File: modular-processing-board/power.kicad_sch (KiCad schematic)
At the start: 10 parts, among them J301 Conn_02x06_Odd_Even, J701 Conn_02x02_Odd_Even, J702 Conn_02x03_Odd_Even, U701 AMS1117-3.3

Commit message: started layout
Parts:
- removed J301: Conn_02x06_Odd_Even, Connector_PinSocket_2.54mm:PinSocket_2x06_P2.54mm_Vertical, symbol Connector_Generic:Conn_02x06_Odd_Even

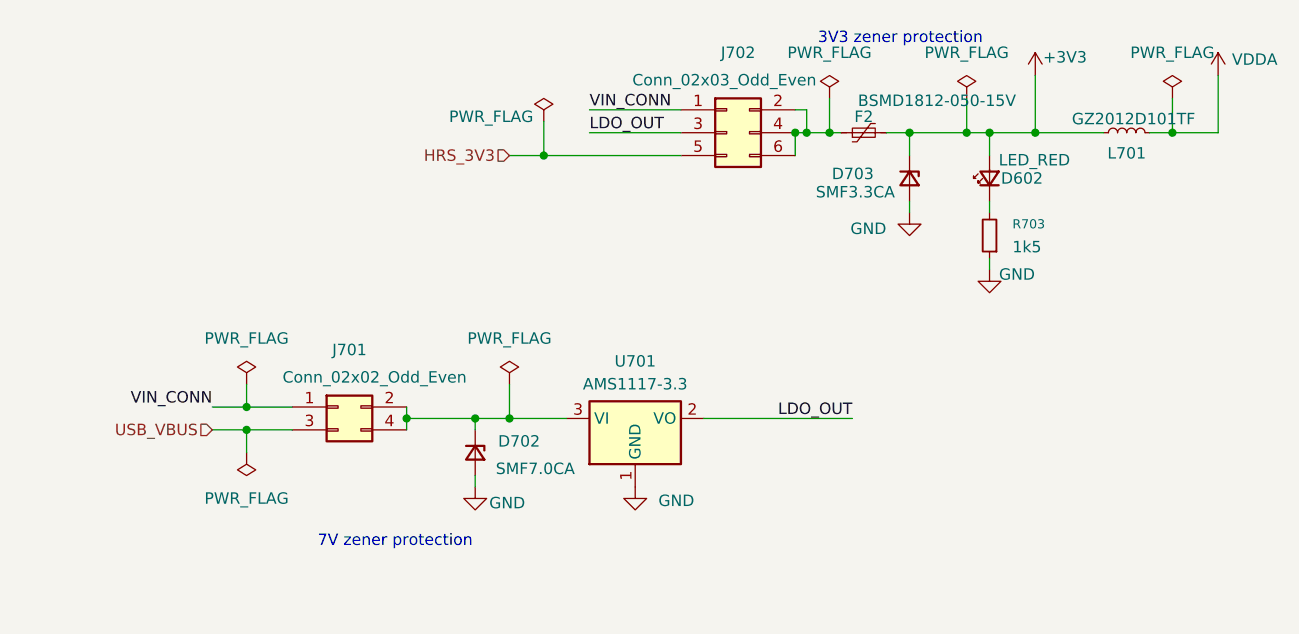
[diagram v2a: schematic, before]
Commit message: removed power input jumpers to single one, added trace impedances and production restrictions (next) route sdram
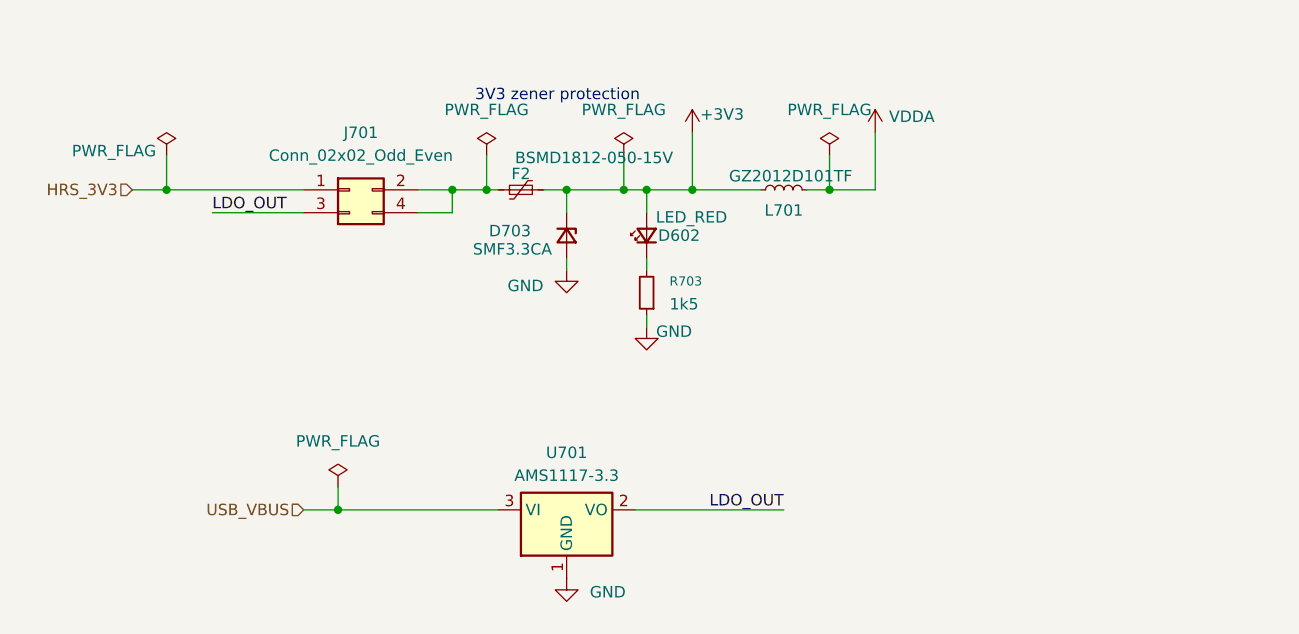
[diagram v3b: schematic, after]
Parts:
- removed D702: SMF7.0CA, Diode_SMD:D_SOD-123F, symbol Device:D_Zener_Small
- removed J702: Conn_02x03_Odd_Even, Connector_PinHeader_2.54mm:PinHeader_2x03_P2.54mm_Vertical, symbol Connector_Generic:Conn_02x03_Odd_Even
- J701: LPN C66690 -> (none); MPN 2.54-2*2PPin -> (none)
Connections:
- net VIN_CONN is gone; now on net HRS_3V3: J701.1 (Pin_1)
- net LDO_OUT: now also J701.3 (Pin_3)
- net USB_VBUS: now also U701.3 (VI); no longer J701.3 (Pin_3)
- net at J701.2 (Pin_2), J701.4 (Pin_4): now also F2.1; no longer U701.3 (VI)
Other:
- note removed: "7V zener protection"
- moved on the sheet: D602, D703, F2, L701, R703, U701

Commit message: figuring out delay matching for sdram
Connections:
- net HRS_3V3: now also J701.3 (Pin_3); no longer J701.1 (Pin_1)
- net LDO_OUT: now also J701.1 (Pin_1); no longer J701.3 (Pin_3)
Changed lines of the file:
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@@
 	)
 	(junction
-		(at 46.99 40.64)
+		(at 46.99 43.18)
 		(diameter 0)
 		(color 0 0 0 0)
@@
 	(wire
 		(pts
-			(xy 43.18 40.64) (xy 46.99 40.64)
-		)
-		(stroke
-			(width 0)
-			(type default)
-		)
-	)
-	(wire
-		(pts
 			(xy 120.65 40.64) (xy 125.73 40.64)
 		)
@@
 	(wire
 		(pts
-			(xy 46.99 36.83) (xy 46.99 40.64)
-		)
-		(stroke
-			(width 0)
-			(type default)
-		)
-	)
-	(wire
-		(pts
 			(xy 91.44 40.64) (xy 97.79 40.64)
 		)
@@
 	(wire
 		(pts
-			(xy 46.99 40.64) (xy 62.23 40.64)
-		)
-		(stroke
-			(width 0)
-			(type default)
-		)
-	)
-	(wire
-		(pts
 			(xy 105.41 40.64) (xy 113.03 40.64)
 		)
@@
 	(wire
 		(pts
-			(xy 52.07 43.18) (xy 62.23 43.18)
-		)
-		(stroke
-			(width 0)
-			(type default)
-		)
-	)
-	(wire
-		(pts
 			(xy 91.44 48.26) (xy 91.44 49.53)
 		)
@@
 	(wire
 		(pts
+			(xy 46.99 39.37) (xy 46.99 43.18)
+		)
+		(stroke
+			(width 0)
+			(type default)
+		)
+	)
+	(wire
+		(pts
 			(xy 100.33 40.64) (xy 100.33 43.18)
 		)
@@
 	(wire
 		(pts
+			(xy 52.07 40.64) (xy 62.23 40.64)
+		)
+		(stroke
+			(width 0)
+			(type default)
+		)
+	)
+	(wire
+		(pts
+			(xy 46.99 43.18) (xy 62.23 43.18)
+		)
+		(stroke
+			(width 0)
+			(type default)
+		)
+	)
+	(wire
+		(pts
 			(xy 100.33 40.64) (xy 105.41 40.64)
 		)
@@
 	(wire
 		(pts
+			(xy 43.18 43.18) (xy 46.99 43.18)
+		)
+		(stroke
+			(width 0)
+			(type default)
+		)
+	)
+	(wire
+		(pts
 			(xy 118.11 40.64) (xy 120.65 40.64)
 		)
@@
 			(width 0)
 			(type default)
+		)
+	)
+	(label "LDO_OUT"
+		(at 52.07 40.64 0)
+		(effects
+			(font
+				(size 1.27 1.27)
+			)
+			(justify left bottom)
 		)
 	)
@@
 		)
 	)
-	(label "LDO_OUT"
-		(at 52.07 43.18 0)
+	(hierarchical_label "USB_VBUS"
+		(shape input)
+		(at 62.23 76.2 180)
 		(effects
 			(font
 				(size 1.27 1.27)
 			)
-			(justify left bottom)
+			(justify right)
 		)
 	)
 	(hierarchical_label "HRS_3V3"
 		(shape input)
-		(at 43.18 40.64 180)
-		(effects
-			(font
-				(size 1.27 1.27)
-			)
-			(justify right)
-		)
-	)
-	(hierarchical_label "USB_VBUS"
-		(shape input)
-		(at 62.23 76.2 180)
+		(at 43.18 43.18 180)
 		(effects
 			(font
@@
 	(symbol
 		(lib_id "power:PWR_FLAG")
-		(at 46.99 36.83 0)
+		(at 46.99 39.37 0)
 		(unit 1)
 		(exclude_from_sim no)
@@
 		(dnp no)
 		(property "Reference" "#FLG0701"
-			(at 46.99 34.925 0)
+			(at 46.99 37.465 0)
 			(effects
 				(font
@@
 		)
 		(property "Value" "PWR_FLAG"
-			(at 41.148 36.322 0)
+			(at 41.148 38.862 0)
 			(effects
 				(font
@@
 		)
 		(property "Footprint" ""
-			(at 46.99 36.83 0)
+			(at 46.99 39.37 0)
 			(effects
 				(font
@@
 		)
 		(property "Datasheet" "~"
-			(at 46.99 36.83 0)
+			(at 46.99 39.37 0)
 			(effects
 				(font
@@
 		)
 		(property "Description" "Special symbol for telling ERC where power comes from"
-			(at 46.99 36.83 0)
-			(effects
-				(font
+			(at 46.99 39.37 0)
+			(effects
+				(font

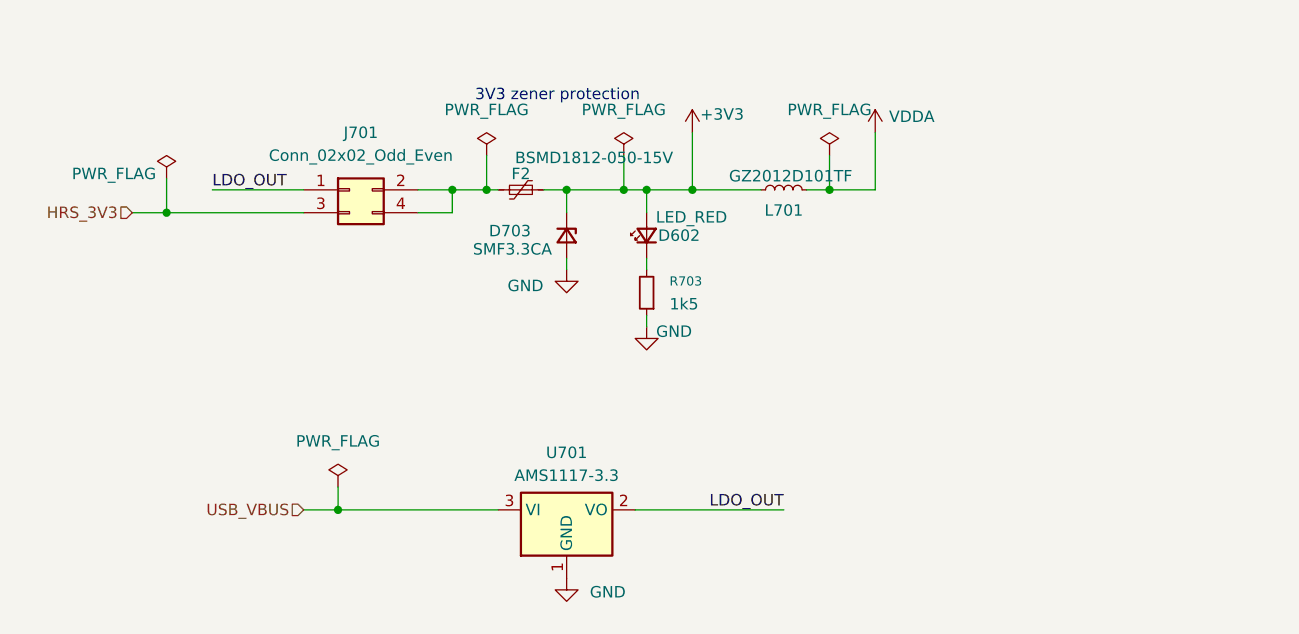
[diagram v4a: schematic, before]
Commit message: finished schematic checks, added extra capacitors on LDO output (next) add holes to board / board shape, do layout checks
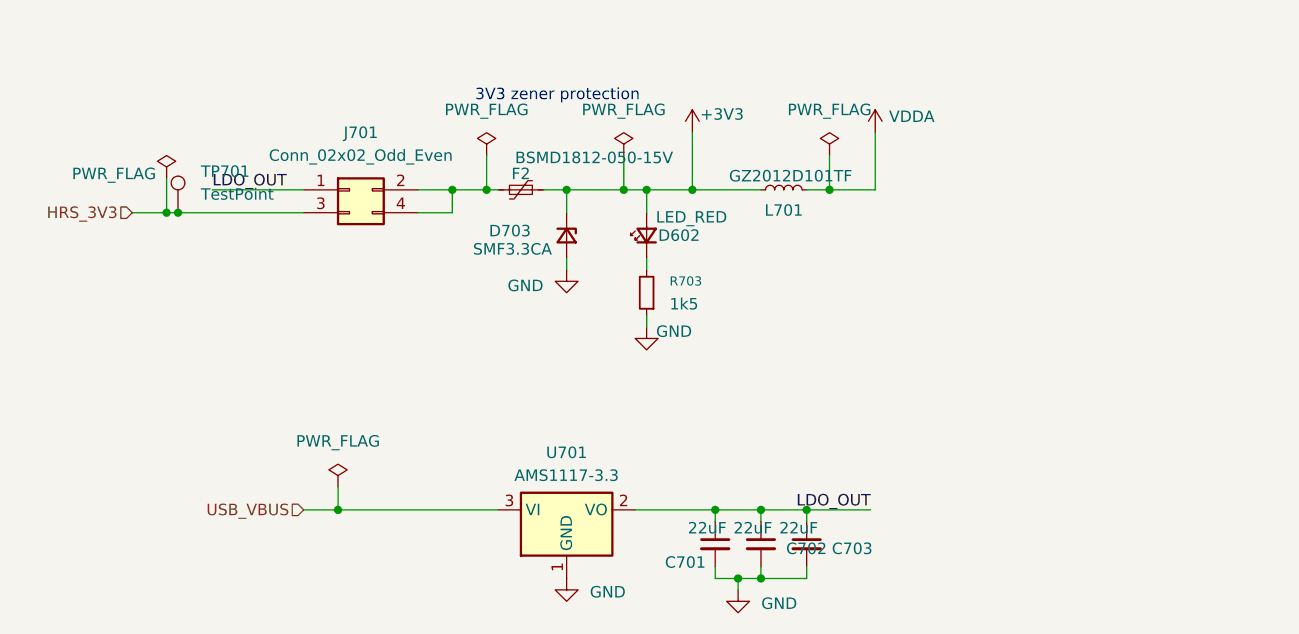
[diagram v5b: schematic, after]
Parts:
- added C701, C702, C703: 22uF, Capacitor_SMD:C_0805_2012Metric, symbol Device:C_Small
- added TP701: TestPoint, iw-misc:TestPoint_Pad_D0.5mm, symbol Connector:TestPoint
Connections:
- net GND: now also C701.2, C702.2, C703.2
- net HRS_3V3: now also TP701.1
- net LDO_OUT: now also C701.1, C702.1, C703.1

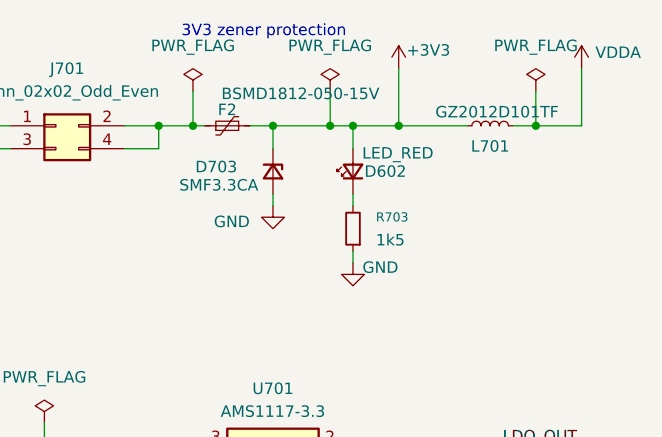
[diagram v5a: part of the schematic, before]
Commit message: checked components part numbers (next) board checks
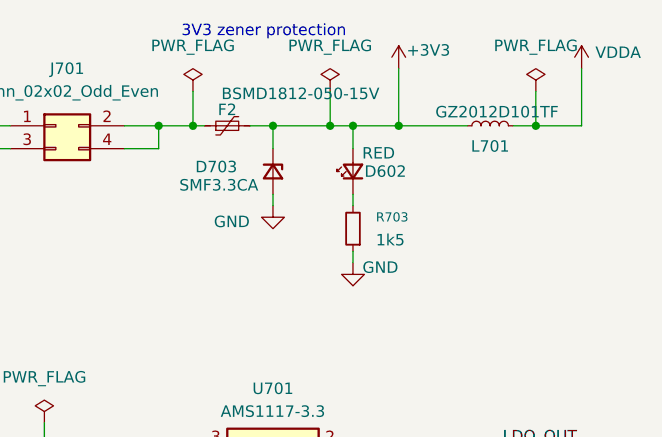
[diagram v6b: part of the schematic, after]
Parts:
- D602: value LED_RED -> RED; LPN (none) -> C2286; MPN (none) -> KT-0603R
- F2: LPN (none) -> C883139; MPN (none) -> BSMD1812-050-15V
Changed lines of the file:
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@@
+			)
+		)
+		(property "LPN" "C883139"
+			(at 86.36 40.64 90)
+			(effects
+				(font
+					(size 1.27 1.27)
+				)
+				(hide yes)
+			)
+		)
+		(property "MPN" "BSMD1812-050-15V "
+			(at 86.36 40.64 90)
+			(effects
+				(font
+					(size 1.27 1.27)
+				)
+				(hide yes)
 			)
 		)
@@
 			)
 		)
-		(property "Value" "LED_RED"
+		(property "Value" "RED"
 			(at 101.346 43.688 90)
 			(effects
@@
 			(effects
 				(font
+					(size 1.27 1.27)
+				)
+				(hide yes)
+			)
+		)
+		(property "LPN" "C2286"
+			(at 100.33 45.72 90)
+			(effects
+				(font
+					(size 1.27 1.27)
+				)
+				(hide yes)
+			)
+		)
+		(property "MPN" "KT-0603R "
+			(at 100.33 45.72 90)
+			(effects
+				(font

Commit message: matched PSSI bus lenghts
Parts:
- D602: LCSC Part Number C2286 -> (none); Manufacturing Part Number KT-0603R -> (none)
- F2: LCSC Part Number C883139 -> (none); Manufacturing part number BSMD1812-050-15V -> (none)
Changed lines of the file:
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@@
-			)
-		)
-		(property "Manufacturing part number" "BSMD1812-050-15V"
-			(at 86.36 40.64 0)
-			(effects
-				(font
-					(size 1.27 1.27)
-				)
-				(hide yes)
-			)
-		)
-		(property "LCSC Part Number" "C883139"
-			(at 86.36 40.64 0)
-			(effects
-				(font
-					(size 1.27 1.27)
-				)
-				(hide yes)
 			)
 		)
@@
 			(effects
 				(font
-					(size 1.27 1.27)
-				)
-				(hide yes)
-			)
-		)
-		(property "LCSC Part Number" "C2286"
-			(at 100.33 45.72 0)
-			(effects
-				(font
-					(size 1.27 1.27)
-				)
-				(hide yes)
-			)
-		)
-		(property "Manufacturing Part Number" "KT-0603R "
-			(at 100.33 45.72 0)
-			(effects
-				(font

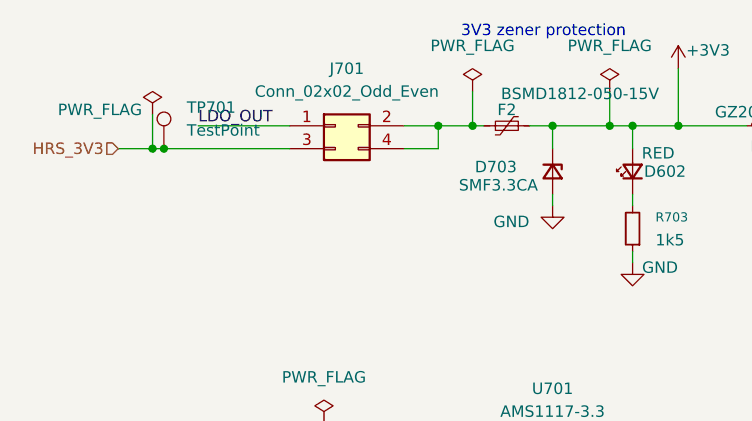
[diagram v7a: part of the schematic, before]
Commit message: minor changes in BOM and DNP-components
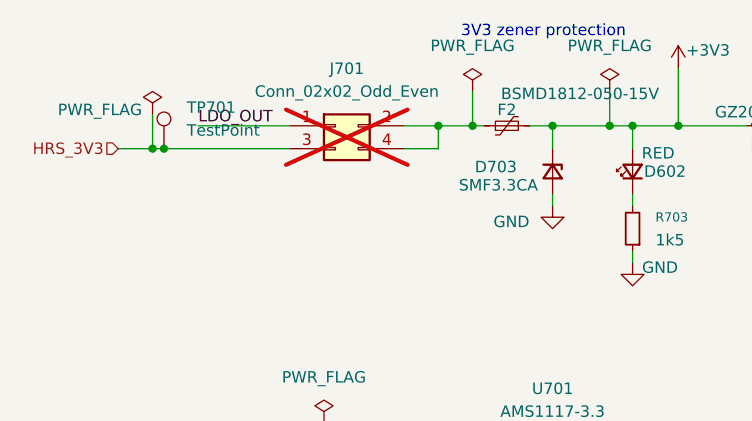
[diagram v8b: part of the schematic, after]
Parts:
- J701: now not fitted; now left out of the parts list
- TP701: now left out of the parts list
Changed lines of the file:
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@@
 		(unit 1)
 		(exclude_from_sim no)
-		(in_bom yes)
+		(in_bom no)
 		(on_board yes)
 		(dnp no)
@@
 		(unit 1)
 		(exclude_from_sim no)
-		(in_bom yes)
-		(on_board yes)
-		(dnp no)
+		(in_bom no)
+		(on_board yes)
+		(dnp yes)
 		(fields_autoplaced yes)
 		(property "Reference" "J701"
